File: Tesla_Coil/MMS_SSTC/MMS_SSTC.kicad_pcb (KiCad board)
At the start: 2 copper layers, 7 parts, among them J2 Screw_Terminal_01x02, Q1 IRFP460APBF

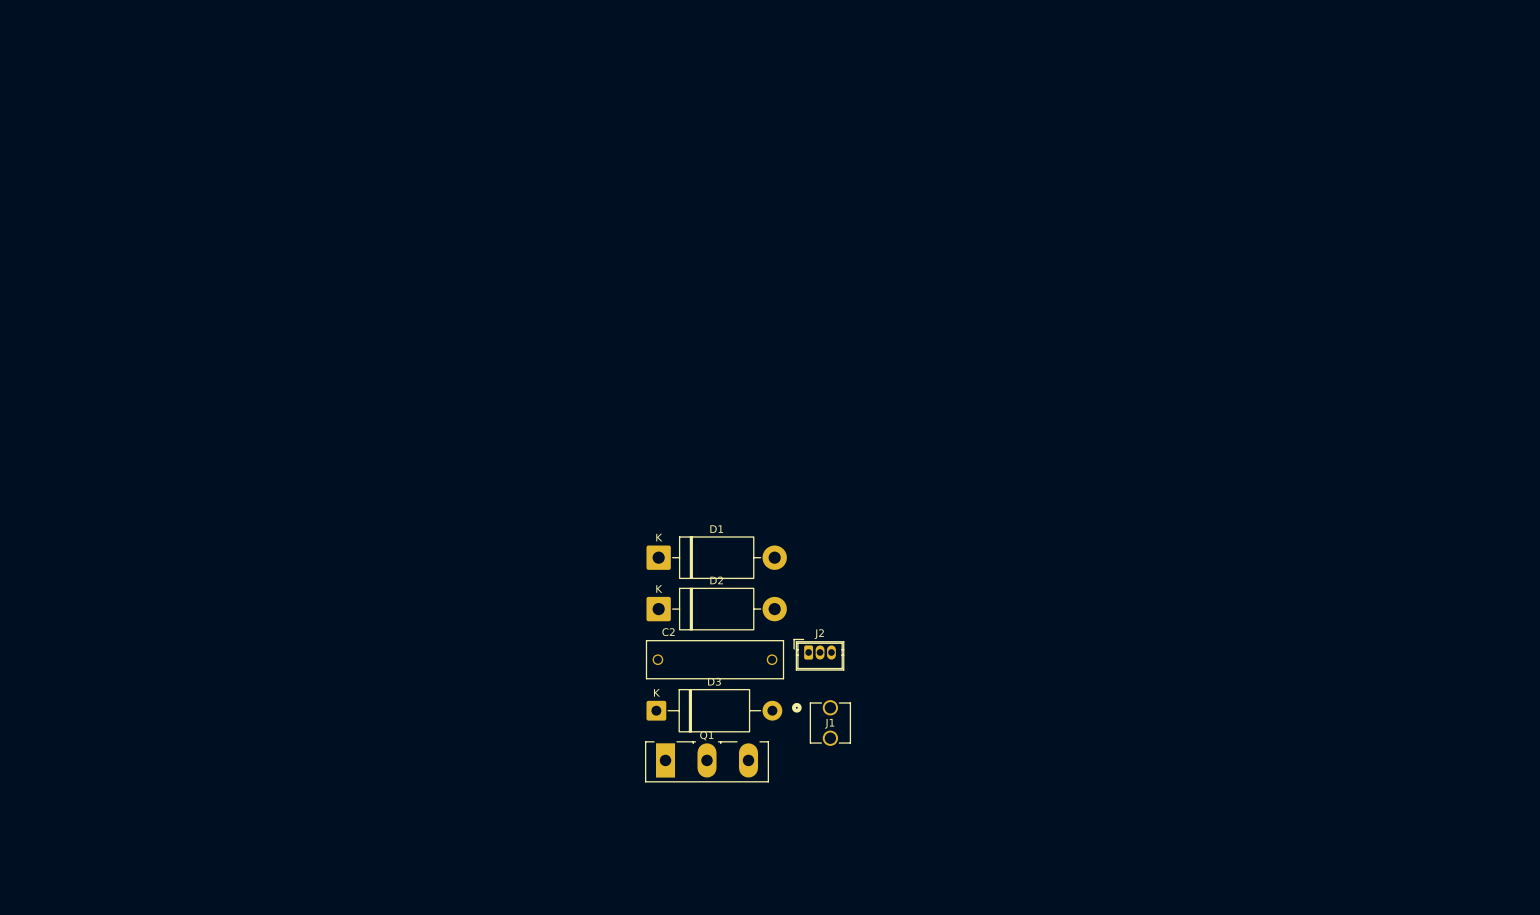
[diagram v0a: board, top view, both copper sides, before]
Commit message: Begin work on SSTC prototype PCB
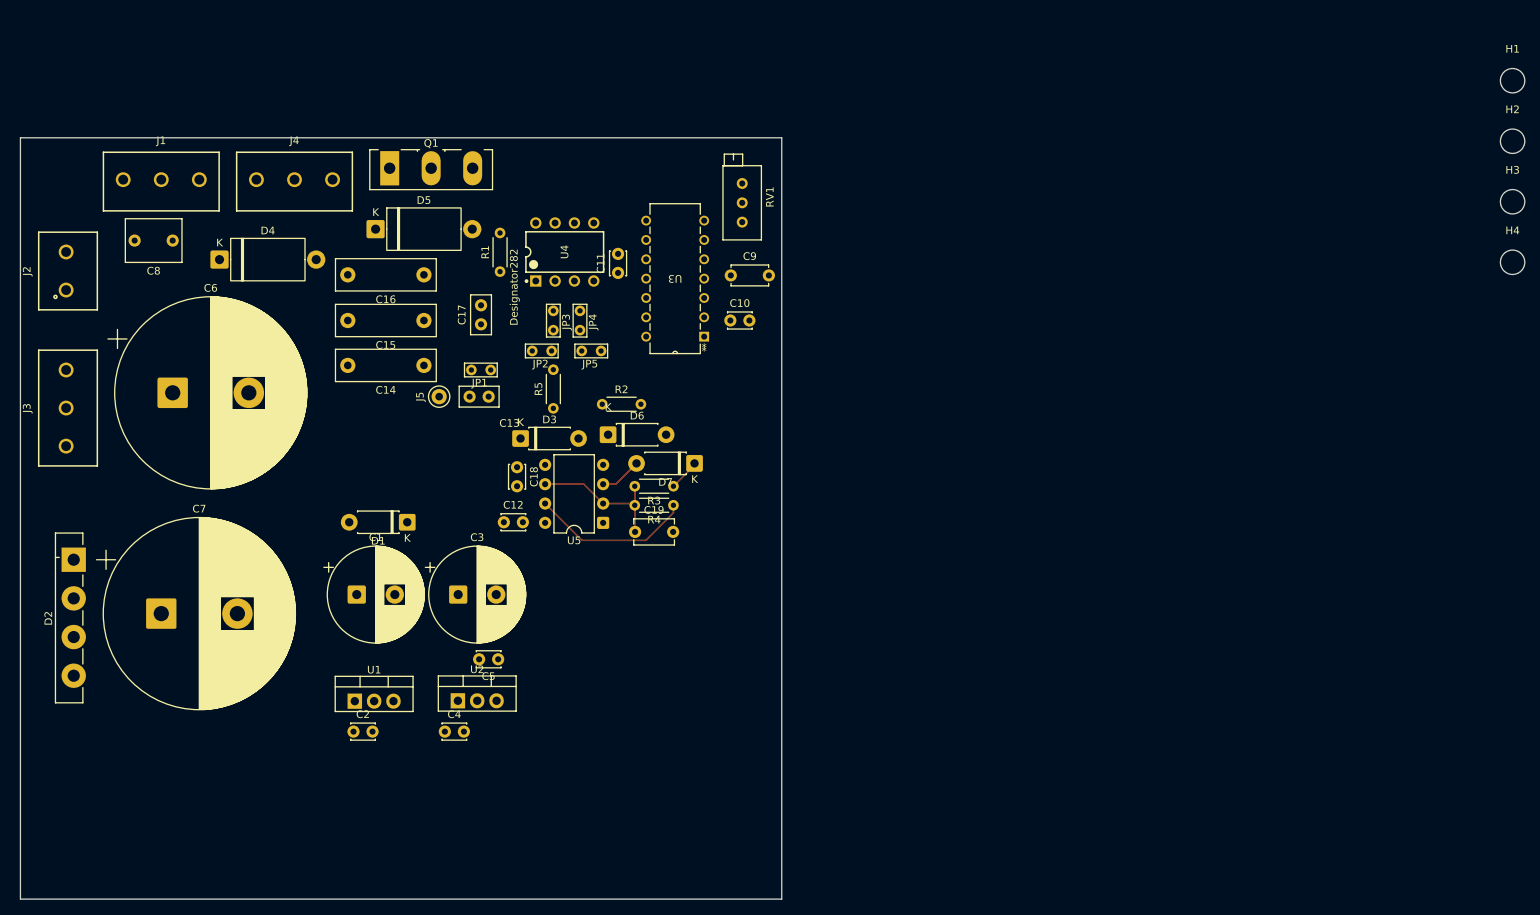
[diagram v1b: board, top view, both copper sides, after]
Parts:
- added C1: 470u, Capacitor_THT:CP_Radial_D12.5mm_P5.00mm, F.Cu at (103.7, 89.0)
- added C10: 0.1u, Capacitor_THT:C_Disc_D3.0mm_W2.0mm_P2.50mm, F.Cu at (152.8, 53.0)
- added C11: 0.1u, Capacitor_THT:C_Disc_D3.0mm_W2.0mm_P2.50mm, F.Cu at (138.0, 46.8)
- added C12: 0.1u, Capacitor_THT:C_Disc_D3.0mm_W2.0mm_P2.50mm, F.Cu at (123.0, 79.5)
- added C13: 10n, Capacitor_THT:C_Disc_D5.0mm_W2.5mm_P2.50mm, F.Cu at (121.0, 63.0)
- added C14: 1.5n, Capacitor_THT:C_Rect_L13.0mm_W4.0mm_P10.00mm_FKS3_FKP3_MKS4, F.Cu at (112.5, 58.9)
- added C15: 1.5n, Capacitor_THT:C_Rect_L13.0mm_W4.0mm_P10.00mm_FKS3_FKP3_MKS4, F.Cu at (112.5, 53.0)
- added C16: 1.5n, Capacitor_THT:C_Rect_L13.0mm_W4.0mm_P10.00mm_FKS3_FKP3_MKS4, F.Cu at (112.5, 47.0)
- added C17: 10n, Capacitor_THT:C_Disc_D5.0mm_W2.5mm_P2.50mm, F.Cu at (120.0, 53.5)
- added C18: 0.1u, Capacitor_THT:C_Disc_D3.0mm_W2.0mm_P2.50mm, F.Cu at (124.7, 72.3)
- added C19: 330n, Capacitor_THT:C_Disc_D5.1mm_W3.2mm_P5.00mm, F.Cu at (140.2, 80.8)
- added C3: 470u, Capacitor_THT:CP_Radial_D12.5mm_P5.00mm, F.Cu at (117.0, 89.0)
- added C4: 0.1u, Capacitor_THT:C_Disc_D3.0mm_W2.0mm_P2.50mm, F.Cu at (115.2, 107.0)
- added C5: 0.1u, Capacitor_THT:C_Disc_D3.0mm_W2.0mm_P2.50mm, F.Cu at (122.2, 97.5)
- added C6: 2200u, Capacitor_THT:CP_Radial_D25.0mm_P10.00mm_SnapIn, F.Cu at (79.5, 62.5)
- added C7: 2200u, Capacitor_THT:CP_Radial_D25.0mm_P10.00mm_SnapIn, F.Cu at (78.0, 91.5)
- added C8: 0.68u, Capacitor_THT:C_Rect_L7.2mm_W5.5mm_P5.00mm_FKS2_FKP2_MKS2_MKP2, F.Cu at (79.5, 42.5)
- added C9: 470p, Capacitor_THT:C_Disc_D4.7mm_W2.5mm_P5.00mm, F.Cu at (152.8, 47.1)
- added D4: 400V, Diode_THT:D_DO-27_P12.70mm_Horizontal, F.Cu at (85.7, 45.0)
- added D5: 18V, Diode_THT:D_DO-27_P12.70mm_Horizontal, F.Cu at (106.2, 41.0)
- added D6: ~, Diode_THT:D_DO-41_SOD81_P7.62mm_Horizontal, F.Cu at (136.7, 68.0)
- added D7: D_Filled, Diode_THT:D_DO-41_SOD81_P7.62mm_Horizontal, F.Cu at (148.0, 71.8)
- added H1: MountingHole, MountingHole:MountingHole_3.2mm_M3, F.Cu at (255.5, 21.5)
- added H2: MountingHole, MountingHole:MountingHole_3.2mm_M3, F.Cu at (255.5, 29.4)
- added H3: MountingHole, MountingHole:MountingHole_3.2mm_M3, F.Cu at (255.5, 37.4)
- added H4: MountingHole, MountingHole:MountingHole_3.2mm_M3, F.Cu at (255.5, 45.4)
- added J3: Screw_Terminal_01x02, locals:691137710003, F.Cu at (65.5, 64.5)
- added J4: Screw_Terminal_01x02, locals:691137710003, F.Cu at (95.5, 34.5)
- added J5: Wire_Solder_Point, TestPoint:TestPoint_Keystone_5000-5004_Miniature, F.Cu at (114.5, 63.0)
- added JP1: Jumper_2_Bridged, TestPoint:TestPoint_Bridge_Pitch2.54mm_Drill0.7mm, F.Cu at (118.7, 59.5)
- added JP2: Jumper_2_Open, TestPoint:TestPoint_Bridge_Pitch2.54mm_Drill0.7mm, F.Cu at (126.7, 57.0)
- added JP3: Jumper_2_Bridged, TestPoint:TestPoint_Bridge_Pitch2.54mm_Drill0.7mm, F.Cu at (129.5, 54.3)
- added JP4: Jumper_2_Bridged, TestPoint:TestPoint_Bridge_Pitch2.54mm_Drill0.7mm, F.Cu at (133.0, 54.3)
- added JP5: Jumper_2_Open, TestPoint:TestPoint_Bridge_Pitch2.54mm_Drill0.7mm, F.Cu at (133.2, 57.0)
- added R1: 1.5R, Resistor_THT:R_Axial_DIN0204_L3.6mm_D1.6mm_P5.08mm_Horizontal, F.Cu at (122.5, 46.6)
- added R2: 220k, Resistor_THT:R_Axial_DIN0204_L3.6mm_D1.6mm_P5.08mm_Horizontal, F.Cu at (135.9, 64.0)
- added R3: 22k, Resistor_THT:R_Axial_DIN0204_L3.6mm_D1.6mm_P5.08mm_Horizontal, F.Cu at (145.3, 74.8)
- added R4: 150k, Resistor_THT:R_Axial_DIN0204_L3.6mm_D1.6mm_P5.08mm_Horizontal, F.Cu at (145.3, 77.3)
- added R5: 1k, Resistor_THT:R_Axial_DIN0204_L3.6mm_D1.6mm_P5.08mm_Horizontal, F.Cu at (129.5, 64.5)
- added RV1: 10k, Potentiometer_THT:Potentiometer_Bourns_3296X_Horizontal, F.Cu at (154.3, 40.1)
- added U1: LM7812_TO220, Package_TO_SOT_THT:TO-220-3_Vertical, F.Cu at (103.4, 103.0)
- added U2: LM7805_TO220, Package_TO_SOT_THT:TO-220-3_Vertical, F.Cu at (117.0, 103.0)
- added U3: CD74HC14E, locals:N14, F.Cu at (141.7, 39.9)
- added U4: UCC27524P, locals:P0008A, F.Cu at (131.0, 44.0)
- added U5: NE555P, Package_DIP:DIP-8_W7.62mm, F.Cu at (136.0, 79.6)
- C2: value 100n -> 0.1u; footprint locals:CAPRR1500W80L1800T500H1050 -> Capacitor_THT:C_Disc_D3.0mm_W2.0mm_P2.50mm
- D1: footprint Diode_THT:D_DO-201AD_P15.24mm_Horizontal -> Diode_THT:D_DO-41_SOD81_P7.62mm_Horizontal
- D2: value 5A+ please -> B125C2300-1500A; footprint Diode_THT:D_DO-201AD_P15.24mm_Horizontal -> Diode_THT:Diode_Bridge_Vishay_GBU
- D3: value P6KE13CA -> ~; footprint Diode_THT:D_DO-201AE_P15.24mm_Horizontal -> Diode_THT:D_DO-41_SOD81_P7.62mm_Horizontal
- J1: value ~ -> Screw_Terminal_01x02; footprint locals:CONN_360410_MZC -> locals:691137710003
- J2: footprint Connector_Wuerth:Wuerth_WR-WTB_64800311622_1x03_P1.50mm_Vertical -> locals:691137710002
- moved J1 112.0 mm to (78.0, 34.5)
- moved J2 109.7 mm to (65.5, 46.5), turned to 90 degrees
- moved Q1 85.8 mm to (108.0, 33.0)
- moved D2 77.1 mm to (66.5, 84.4), turned to -90 degrees
- moved C2 48.4 mm to (103.2, 107.0)
- moved D3 40.0 mm to (125.2, 68.5)
- moved D1 33.3 mm to (110.3, 79.5), turned to 180 degrees
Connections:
- C2 pad 2: GND -> Earth
- D1 pad 2: Net-(D1-A) -> 24VAC
- D2 pad 1: Net-(D1-A) -> Earth
- D2 pad 2: GND -> 0VAC
- D3 pad 1: GND -> +12V
- D3 pad 2: /secondary -> Net-(D3-A)
- J1 pad 1: /secondary -> HT
- J1 pad 2: (no net) -> NEUT
- J2 pad 1: AC -> HT
- J2 pad 2: Earth -> NEUT
- Q1 pad 1: /secondary -> Net-(D5-A2)
- Q1 pad 3: GND -> Earth
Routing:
- net Net-(U5-DIS): track 0.00 -> 21.3 mm
- net Net-(U5-THR): track 0.00 -> 18.9 mm
- net Net-(D7-A): track 0.00 -> 5.52 mm
- net Net-(D7-K): track 0.00 -> 4.15 mm
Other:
- board outline added: 100 x 100 mm
- copper layers 2 -> 4

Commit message: Finish SSTC prototype PCB
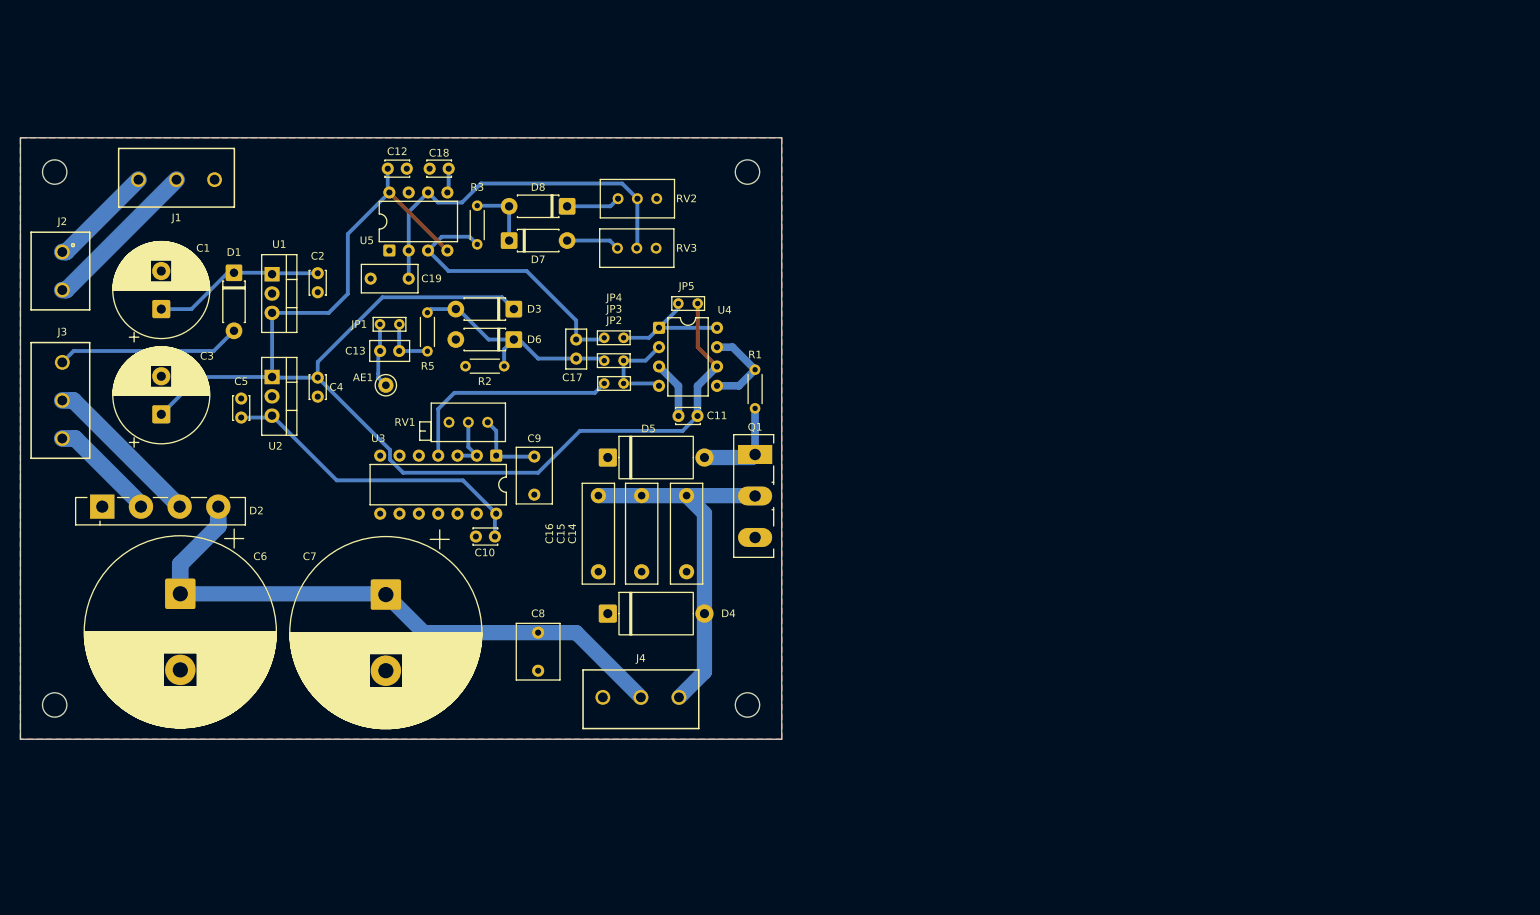
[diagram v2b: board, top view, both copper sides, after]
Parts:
- removed J5: Wire_Solder_Point, TestPoint:TestPoint_Keystone_5000-5004_Miniature
- removed R4: 150k, Resistor_THT:R_Axial_DIN0204_L3.6mm_D1.6mm_P5.08mm_Horizontal
- added AE1: Antenna, TestPoint:TestPoint_Keystone_5000-5004_Miniature, F.Cu at (107.5, 61.5)
- added D8: D_Small_Filled, Diode_THT:D_DO-41_SOD81_P7.62mm_Horizontal, F.Cu at (123.7, 42.5)
- added RV2: R_Potentiometer_Trim_US, Potentiometer_THT:Potentiometer_Bourns_3296W_Vertical, F.Cu at (138.0, 37.0)
- added RV3: R_Potentiometer_Trim_US, Potentiometer_THT:Potentiometer_Bourns_3296W_Vertical, F.Cu at (137.9, 43.5)
- C19: footprint Capacitor_THT:C_Disc_D5.1mm_W3.2mm_P5.00mm -> Capacitor_THT:C_Rect_L7.2mm_W3.5mm_P5.00mm_FKS2_FKP2_MKS2_MKP2
- C9: footprint Capacitor_THT:C_Disc_D4.7mm_W2.5mm_P5.00mm -> Capacitor_THT:C_Rect_L7.2mm_W4.5mm_P5.00mm_FKS2_FKP2_MKS2_MKP2
- D7: value D_Filled -> D_Small_Filled
- R3: value 22k -> 1k
- U3: footprint locals:N14 -> Package_DIP:DIP-14_W7.62mm
- U4: footprint locals:P0008A -> Package_DIP:DIP-8_W7.62mm
- moved H4 200.1 mm to (64.0, 103.5)
- moved H2 191.5 mm to (64.0, 33.5)
- moved H3 120.3 mm to (155.0, 103.5)
- moved H1 101.2 mm to (155.0, 33.5)
- moved J4 81.8 mm to (141.0, 102.5)
- moved C8 70.4 mm to (127.5, 94.0), turned to -90 degrees
- moved D4 69.0 mm to (136.7, 91.5)
- moved Q1 61.0 mm to (156.0, 70.6), turned to -90 degrees
- moved C2 60.4 mm to (98.5, 46.8), turned to -90 degrees
- moved U1 57.1 mm to (92.5, 46.9), turned to -90 degrees
- moved C4 49.4 mm to (98.5, 60.5), turned to -90 degrees
- moved U2 49.0 mm to (92.5, 60.4), turned to -90 degrees
- moved C12 48.9 mm to (107.8, 33.1)
- moved C5 46.3 mm to (88.5, 65.8), turned to 90 degrees
- moved C3 45.6 mm to (78.0, 65.3), turned to 90 degrees
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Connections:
- net ANT_IN renamed Net-(AE1-A)
- C12 pad 2: GND -> Earth
- C17 pad 2: Net-(D7-A) -> INTERRUPT_OUT
- JP4 pad 1: Net-(D7-A) -> INTERRUPT_OUT
- R3 pad 1: Net-(D7-K) -> INTERRUPT_OUT
- R3 pad 2: Net-(U5-THR) -> Net-(D7-A)
- U3 pad 4: Net-(JP2-B) -> OSC_OUT
- U5 pad 3: Net-(D7-A) -> INTERRUPT_OUT
- U5 pad 7: Net-(U5-DIS) -> Earth
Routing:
- net +12V: track 0.00 -> 179.3 mm
- net +68V: track 0.00 -> 79.8 mm
- net Net-(D4-A2): track 0.00 -> 49.5 mm
- net +5V: track 0.00 -> 42.0 mm
- net INTERRUPT_OUT: track 0.00 -> 37.2 mm
- net Net-(D3-A): track 0.00 -> 30.7 mm
- net Net-(U5-THR): track 18.9 -> 48.8 mm
- net OSC_OUT: track 0.00 -> 29.3 mm
- net 24VAC: track 0.00 -> 24.4 mm
- net Net-(D1-K): track 0.00 -> 22.7 mm
- net Net-(U5-DIS): track 21.3 -> 0.00 mm
- net 48VAC: track 0.00 -> 21.2 mm
- net HT: track 0.00 -> 21.0 mm
- net Net-(JP4-B): track 0.00 -> 17.1 mm
- net 0VAC: track 0.00 -> 14.2 mm
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- added copper zone on B.Cu, net Earth
- added copper zone on F.Cu, net Earth
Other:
- board size 100 x 100 mm -> 100 x 79 mm
- copper layers 4 -> 2

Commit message: Commit minor changes to SSTC
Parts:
- RV1: footprint Potentiometer_THT:Potentiometer_Bourns_3296X_Horizontal -> Potentiometer_THT:Potentiometer_Bourns_3296W_Vertical
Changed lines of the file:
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@@
 			(plot_on_all_layers_selection 0x00000000_00000000_00000000_00000000)
 			(disableapertmacros no)
-			(usegerberextensions no)
-			(usegerberattributes yes)
-			(usegerberadvancedattributes yes)
+			(usegerberextensions yes)
+			(usegerberattributes no)
+			(usegerberadvancedattributes no)
 			(creategerberjobfile yes)
 			(dashed_line_dash_ratio 12.000000)
@@
 			(outputformat 1)
 			(mirror no)
-			(drillshape 1)
+			(drillshape 0)
 			(scaleselection 1)
-			(outputdirectory "")
+			(outputdirectory "plots/")
 		)
 	)
@@
 		)
 	)
-	(footprint "Potentiometer_THT:Potentiometer_Bourns_3296X_Horizontal"
+	(footprint "Potentiometer_THT:Potentiometer_Bourns_3296W_Vertical"
 		(layer "F.Cu")
 		(at 120.875 66.37)
-		(descr "Potentiometer, horizontal, Bourns 3296X, https://www.bourns.com/pdfs/3296.pdf")
-		(tags "Potentiometer horizontal Bourns 3296X")
+		(descr "Potentiometer, vertical, Bourns 3296W, https://www.bourns.com/pdfs/3296.pdf")
+		(tags "Potentiometer vertical Bourns 3296W")
 		(property "Reference" "RV1"
-			(at -10.875 0 0)
+			(at -2.54 -3.66 0)
 			(layer "F.SilkS")
 			(effects
@@
 		)
 		(property "Value" "10k"
-			(at -3.3 3.67 0)
+			(at -2.54 3.67 0)
 			(layer "F.Fab")
 			(effects
@@
 			)
 		)
-		(property "DKPN" "3296X-103LF-ND"
+		(property "DKPN" "118-3296W-1-103RLFCT-ND"
 			(at 0 0 0)
 			(unlocked yes)
@@
 		(attr through_hole)
 		(fp_line
-			(start -8.935 -0.055)
-			(end -8.935 2.355)
-			(stroke
-				(width 0.12)
-				(type solid)
-			)
-			(layer "F.SilkS")
-		)
-		(fp_line
-			(start -8.935 -0.055)
-			(end -7.415 -0.055)
-			(stroke
-				(width 0.12)
-				(type solid)
-			)
-			(layer "F.SilkS")
-		)
-		(fp_line
-			(start -8.935 1.15)
-			(end -8.175 1.15)
-			(stroke
-				(width 0.12)
-				(type solid)
-			)
-			(layer "F.SilkS")
-		)
-		(fp_line
-			(start -8.935 2.355)
-			(end -7.415 2.355)
-			(stroke
-				(width 0.12)
-				(type solid)
-			)
-			(layer "F.SilkS")
-		)
-		(fp_line
 			(start -7.415 -2.52)
 			(end -7.415 2.53)
@@
 		)
 		(fp_line
-			(start -7.415 -0.055)
-			(end -7.415 2.355)
-			(stroke
-				(width 0.12)
-				(type solid)
-			)
-			(layer "F.SilkS")
-		)
-		(fp_line
 			(start -7.415 2.53)
 			(end 2.335 2.53)
@@
 		)
 		(fp_rect
-			(start -9.08 -2.66)
+			(start -7.56 -2.66)
 			(end 2.48 2.67)
 			(stroke
@@
 		)
 		(fp_line
-			(start -8.825 1.15)
-			(end -8.065 1.15)
+			(start 1.652 0.32)
+			(end 0.125 1.847)
 			(stroke
 				(width 0.1)
@@
 			(layer "F.Fab")
 		)
-		(fp_rect
-			(start -8.825 0.055)
-			(end -7.305 2.245)
+		(fp_line
+			(start 1.785 0.453)
+			(end 0.258 1.98)
 			(stroke
 				(width 0.1)
 				(type solid)
 			)
-			(fill no)
 			(layer "F.Fab")
 		)
@@
 			(layer "F.Fab")
 		)
+		(fp_circle
+			(center 0.955 1.15)
+			(end 2.05 1.15)
+			(stroke
+				(width 0.1)
+				(type solid)
+			)
+			(fill no)
+			(layer "F.Fab")
+		)
 		(fp_text user "${REFERENCE}"
-			(at -2.54 0.005 0)
+			(at -3.175 0.005 0)
 			(layer "F.Fab")
 			(effects
@@
 		)
 		(embedded_fonts no)
-		(model "${KICAD9_3DMODEL_DIR}/Potentiometer_THT.3dshapes/Potentiometer_Bourns_3296X_Horizontal.step"
+		(model "${KICAD9_3DMODEL_DIR}/Potentiometer_THT.3dshapes/Potentiometer_Bourns_3296W_Vertical.step"
 			(offset
 				(xyz 0 0 0)
@@
 			(pintype "passive")
 			(solder_mask_margin 0.102)
+			(zone_connect 2)
 		)
 		(embedded_fonts no)
@@
 	)
 	(segment
-		(start 117.625 74)
-		(end 121.995 78.37)
+		(start 88.5 65.75)
+		(end 92.3 65.75)
 		(width 0.5)
 		(layer "B.Cu")
@@
 	)
 	(segment
-		(start 101.05 74)
-		(end 117.625 74)
+		(start 117.625 74)
+		(end 121.995 78.37)
 		(width 0.5)
 		(layer "B.Cu")
@@
 	)
 	(segment
-		(start 88.5 65.75)
-		(end 92.3 65.75)
+		(start 121.825 78.54)
+		(end 121.995 78.37)
 		(width 0.5)
 		(layer "B.Cu")
@@
 	)
 	(segment
-		(start 121.825 78.54)
-		(end 121.995 78.37)
+		(start 92.3 65.75)
+		(end 92.55 65.5)
 		(width 0.5)
 		(layer "B.Cu")
@@
 	)
 	(segment
-		(start 92.3 65.75)
-		(end 92.55 65.5)
+		(start 101.05 74)
+		(end 117.625 74)
 		(width 0.5)
 		(layer "B.Cu")
